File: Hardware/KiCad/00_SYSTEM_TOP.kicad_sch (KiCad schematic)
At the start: 0 parts

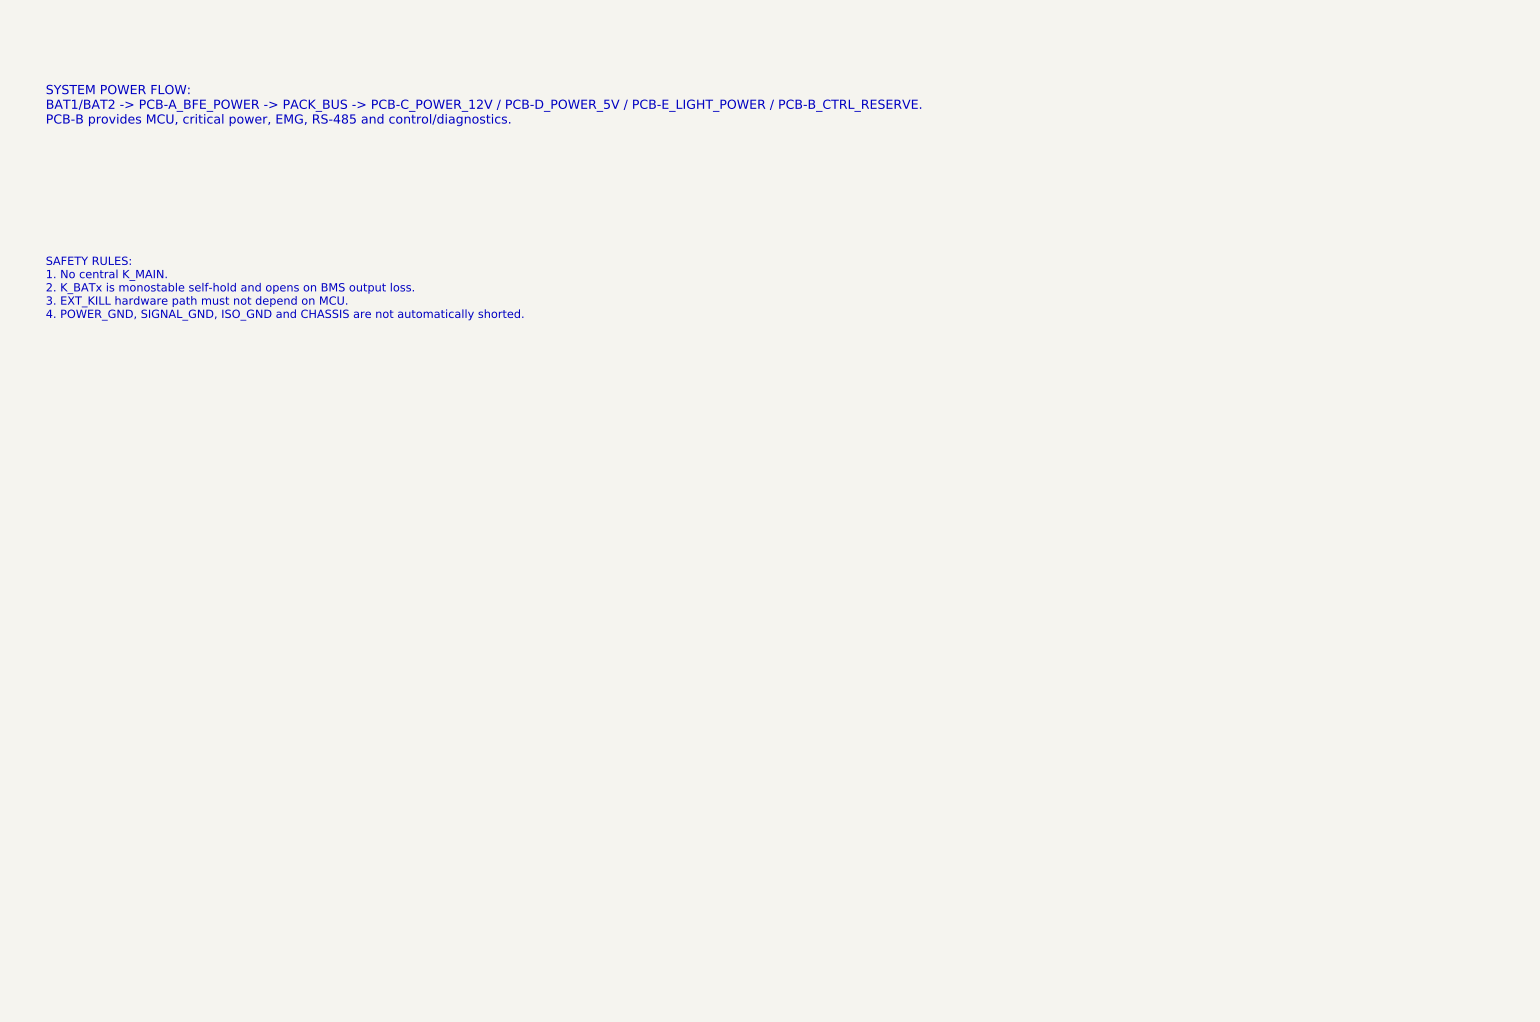
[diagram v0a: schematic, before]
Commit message: hardware: detail 00_SYSTEM_TOP architecture sheet
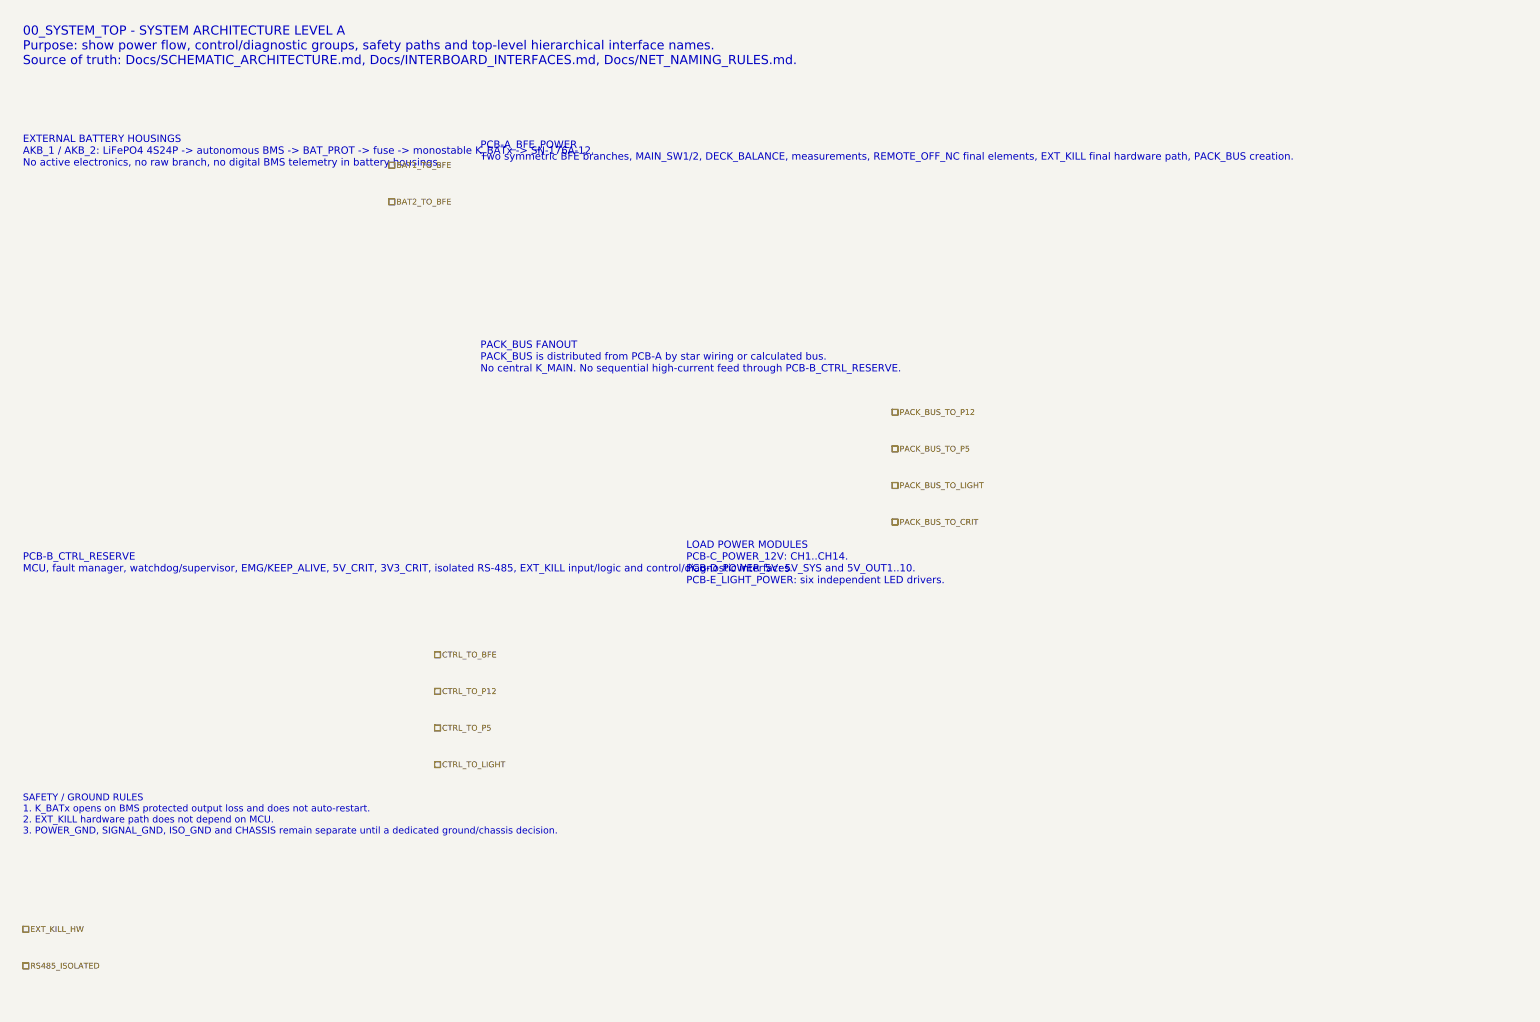
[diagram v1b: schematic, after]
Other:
- note added: "00_SYSTEM_TOP - SYSTEM ARCHITECTURE LEVEL A Purpose: show power flow, control/diagnostic groups, safety paths and top-level hierarchical interface names. Source of truth: Docs/SCHEMATIC_ARCHITECTURE.md, Docs/INTERBOARD_INTERFACES.md, Docs/NET_NAMING_RULES.md."
- note added: "EXTERNAL BATTERY HOUSINGS AKB_1 / AKB_2: LiFePO4 4S24P -> autonomous BMS -> BAT_PROT -> fuse -> monostable K_BATx -> SN-176A-12. No active electronics, no raw branch, no digital BMS telemetry in battery housings."
- note added: "LOAD POWER MODULES PCB-C_POWER_12V: CH1..CH14. PCB-D_POWER_5V: 5V_SYS and 5V_OUT1..10. PCB-E_LIGHT_POWER: six independent LED drivers."
- note added: "PACK_BUS FANOUT PACK_BUS is distributed from PCB-A by star wiring or calculated bus. No central K_MAIN. No sequential high-current feed through PCB-B_CTRL_RESERVE."
- note added: "PCB-A_BFE_POWER Two symmetric BFE branches, MAIN_SW1/2, DECK_BALANCE, measurements, REMOTE_OFF_NC final elements, EXT_KILL final hardware path, PACK_BUS creation."
- note added: "PCB-B_CTRL_RESERVE MCU, fault manager, watchdog/supervisor, EMG/KEEP_ALIVE, 5V_CRIT, 3V3_CRIT, isolated RS-485, EXT_KILL input/logic and control/diagnostic interfaces."
- note added: "SAFETY / GROUND RULES 1. K_BATx opens on BMS protected output loss and does not auto-restart. 2. EXT_KILL hardware path does not depend on MCU. 3. POWER_GND, SIGNAL_GND, ISO_GND and CHASSIS remain separate until a dedicated ground/chassis decision."
- note removed: "SAFETY RULES: 1. No central K_MAIN. 2. K_BATx is monostable self-hold and opens on BMS output loss. 3. EXT_KILL hardware path must not depend on MCU. 4. POWER_GND, SIGNAL_GND, ISO_GND and CHASSIS are not automatically shorted."
- note removed: "SYSTEM POWER FLOW: BAT1/BAT2 -> PCB-A_BFE_POWER -> PACK_BUS -> PCB-C_POWER_12V / PCB-D_POWER_5V / PCB-E_LIGHT_POWER / PCB-B_CTRL_RESERVE. PCB-B provides MCU, critical power, EMG, RS-485 and control/diagnostics."
- company: (none) -> Gonoboben/plataVM
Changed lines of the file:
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@@
 	(title_block
 		(title "00_SYSTEM_TOP - PlataVM system overview")
-		(date "2026-07-14")
-		(rev "A0")
-		(comment 1 "Architecture level A: functional hierarchy, no part numbers")
-	)
-	(text "SYSTEM POWER FLOW:\nBAT1/BAT2 -> PCB-A_BFE_POWER -> PACK_BUS -> PCB-C_POWER_12V / PCB-D_POWER_5V / PCB-E_LIGHT_POWER / PCB-B_CTRL_RESERVE.\nPCB-B provides MCU, critical power, EMG, RS-485 and control/diagnostics."
-		(exclude_from_sim no)
-		(at 20 25 0)
+		(date "2026-07-15")
+		(rev "A1")
+		(company "Gonoboben/plataVM")
+		(comment 1 "Architecture Level A: functional blocks and hierarchical labels")
+		(comment 2 "No part numbers, footprints or PCB layout selected on this sheet")
+	)
+	(text "00_SYSTEM_TOP - SYSTEM ARCHITECTURE LEVEL A\nPurpose: show power flow, control/diagnostic groups, safety paths and top-level hierarchical interface names.\nSource of truth: Docs/SCHEMATIC_ARCHITECTURE.md, Docs/INTERBOARD_INTERFACES.md, Docs/NET_NAMING_RULES.md."
+		(exclude_from_sim no)
+		(at 15 12 0)
 		(effects
 			(font
@@
 		)
 	)
-	(text "SAFETY RULES:\n1. No central K_MAIN.\n2. K_BATx is monostable self-hold and opens on BMS output loss.\n3. EXT_KILL hardware path must not depend on MCU.\n4. POWER_GND, SIGNAL_GND, ISO_GND and CHASSIS are not automatically shorted."
-		(exclude_from_sim no)
-		(at 20 65 0)
-		(effects
-			(font
-				(size 1.8 1.8)
-			)
-			(justify left)
+	(text "EXTERNAL BATTERY HOUSINGS\nAKB_1 / AKB_2: LiFePO4 4S24P -> autonomous BMS -> BAT_PROT -> fuse -> monostable K_BATx -> SN-176A-12.\nNo active electronics, no raw branch, no digital BMS telemetry in battery housings."
+		(exclude_from_sim no)
+		(at 15 35 0)
+		(effects
+			(font
+				(size 1.6 1.6)
+			)
+			(justify left)
+		)
+	)
+	(text "PCB-A_BFE_POWER\nTwo symmetric BFE branches, MAIN_SW1/2, DECK_BALANCE, measurements, REMOTE_OFF_NC final elements, EXT_KILL final hardware path, PACK_BUS creation."
+		(exclude_from_sim no)
+		(at 115 35 0)
+		(effects
+			(font
+				(size 1.6 1.6)
+			)
+			(justify left)
+		)
+	)
+	(text "PACK_BUS FANOUT\nPACK_BUS is distributed from PCB-A by star wiring or calculated bus.\nNo central K_MAIN. No sequential high-current feed through PCB-B_CTRL_RESERVE."
+		(exclude_from_sim no)
+		(at 115 80 0)
+		(effects
+			(font
+				(size 1.6 1.6)
+			)
+			(justify left)
+		)
+	)
+	(text "PCB-B_CTRL_RESERVE\nMCU, fault manager, watchdog/supervisor, EMG/KEEP_ALIVE, 5V_CRIT, 3V3_CRIT, isolated RS-485, EXT_KILL input/logic and control/diagnostic interfaces."
+		(exclude_from_sim no)
+		(at 15 125 0)
+		(effects
+			(font
+				(size 1.6 1.6)
+			)
+			(justify left)
+		)
+	)
+	(text "LOAD POWER MODULES\nPCB-C_POWER_12V: CH1..CH14.\nPCB-D_POWER_5V: 5V_SYS and 5V_OUT1..10.\nPCB-E_LIGHT_POWER: six independent LED drivers."
+		(exclude_from_sim no)
+		(at 160 125 0)
+		(effects
+			(font
+				(size 1.6 1.6)
+			)
+			(justify left)
+		)
+	)
+	(text "SAFETY / GROUND RULES\n1. K_BATx opens on BMS protected output loss and does not auto-restart.\n2. EXT_KILL hardware path does not depend on MCU.\n3. POWER_GND, SIGNAL_GND, ISO_GND and CHASSIS remain separate until a dedicated ground/chassis decision."
+		(exclude_from_sim no)
+		(at 15 180 0)
+		(effects
+			(font
+				(size 1.5 1.5)
+			)
+			(justify left)
+		)
+	)
+	(hierarchical_label "BAT1_TO_BFE"
+		(shape passive)
+		(exclude_from_sim no)
+		(at 95 38 0)
+		(effects
+			(font
+				(size 1.27 1.27)
+			)
+			(justify left)
+		)
+	)
+	(hierarchical_label "BAT2_TO_BFE"
+		(shape passive)
+		(exclude_from_sim no)
+		(at 95 46 0)
+		(effects
+			(font
+				(size 1.27 1.27)
+			)
+			(justify left)
+		)
+	)
+	(hierarchical_label "PACK_BUS_TO_P12"
+		(shape passive)
+		(exclude_from_sim no)
+		(at 205 92 0)
+		(effects
+			(font
+				(size 1.27 1.27)
+			)
+			(justify left)
+		)
+	)
+	(hierarchical_label "PACK_BUS_TO_P5"
+		(shape passive)
+		(exclude_from_sim no)
+		(at 205 100 0)
+		(effects
+			(font
+				(size 1.27 1.27)
+			)
+			(justify left)
+		)
+	)
+	(hierarchical_label "PACK_BUS_TO_LIGHT"
+		(shape passive)
+		(exclude_from_sim no)
+		(at 205 108 0)
+		(effects
+			(font
+				(size 1.27 1.27)
+			)
+			(justify left)
+		)
+	)
+	(hierarchical_label "PACK_BUS_TO_CRIT"
+		(shape passive)
+		(exclude_from_sim no)
+		(at 205 116 0)
+		(effects
+			(font
+				(size 1.27 1.27)
+			)
+			(justify left)
+		)
+	)
+	(hierarchical_label "CTRL_TO_BFE"
+		(shape passive)
+		(exclude_from_sim no)
+		(at 105 145 0)
+		(effects
+			(font
+				(size 1.27 1.27)
+			)
+			(justify left)
+		)
+	)
+	(hierarchical_label "CTRL_TO_P12"
+		(shape passive)
+		(exclude_from_sim no)
+		(at 105 153 0)
+		(effects
+			(font
+				(size 1.27 1.27)
+			)
+			(justify left)
+		)
+	)
+	(hierarchical_label "CTRL_TO_P5"
+		(shape passive)
+		(exclude_from_sim no)
+		(at 105 161 0)
+		(effects
+			(font
+				(size 1.27 1.27)
+			)
+			(justify left)
+		)
+	)
+	(hierarchical_label "CTRL_TO_LIGHT"
+		(shape passive)
+		(exclude_from_sim no)
+		(at 105 169 0)
+		(effects
+			(font
+				(size 1.27 1.27)
+			)
+			(justify left)
+		)
+	)
+	(hierarchical_label "EXT_KILL_HW"
+		(shape passive)
+		(exclude_from_sim no)
+		(at 15 205 0)
+		(effects
+			(font
+				(size 1.27 1.27)
+			)
+			(justify left)
+		)
+	)
+	(hierarchical_label "RS485_ISOLATED"
+		(shape passive)
+		(exclude_from_sim no)
+		(at 15 213 0)
+		(effects
+			(font
+				(size 1.27 1.27)
+			)
+			(justify left)
